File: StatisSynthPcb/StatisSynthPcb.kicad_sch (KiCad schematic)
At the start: 6 parts, among them SW1 SW_Push, SW2 SW_Push

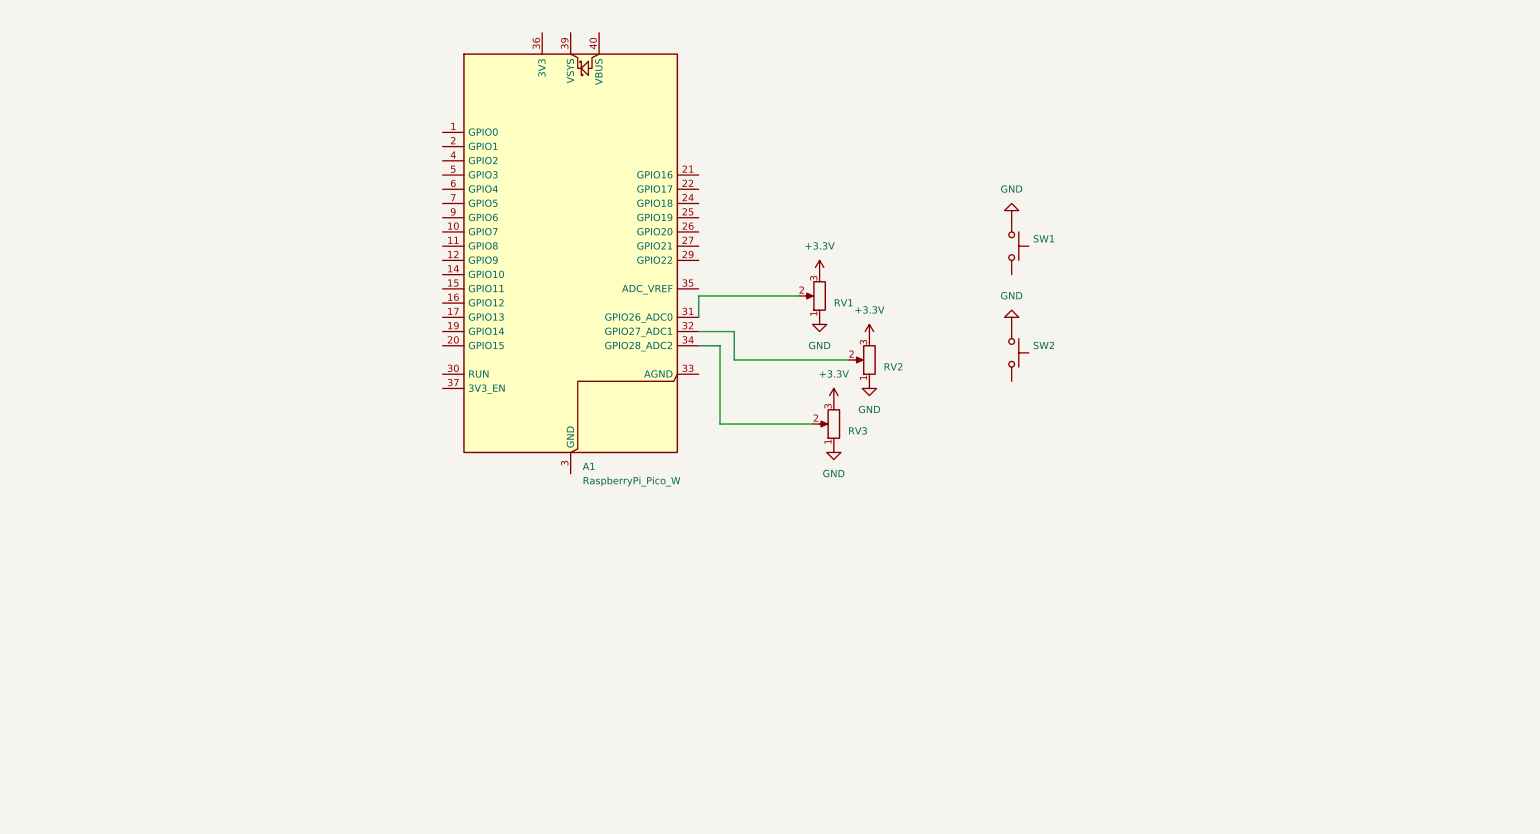
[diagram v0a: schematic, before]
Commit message: made first pcb version
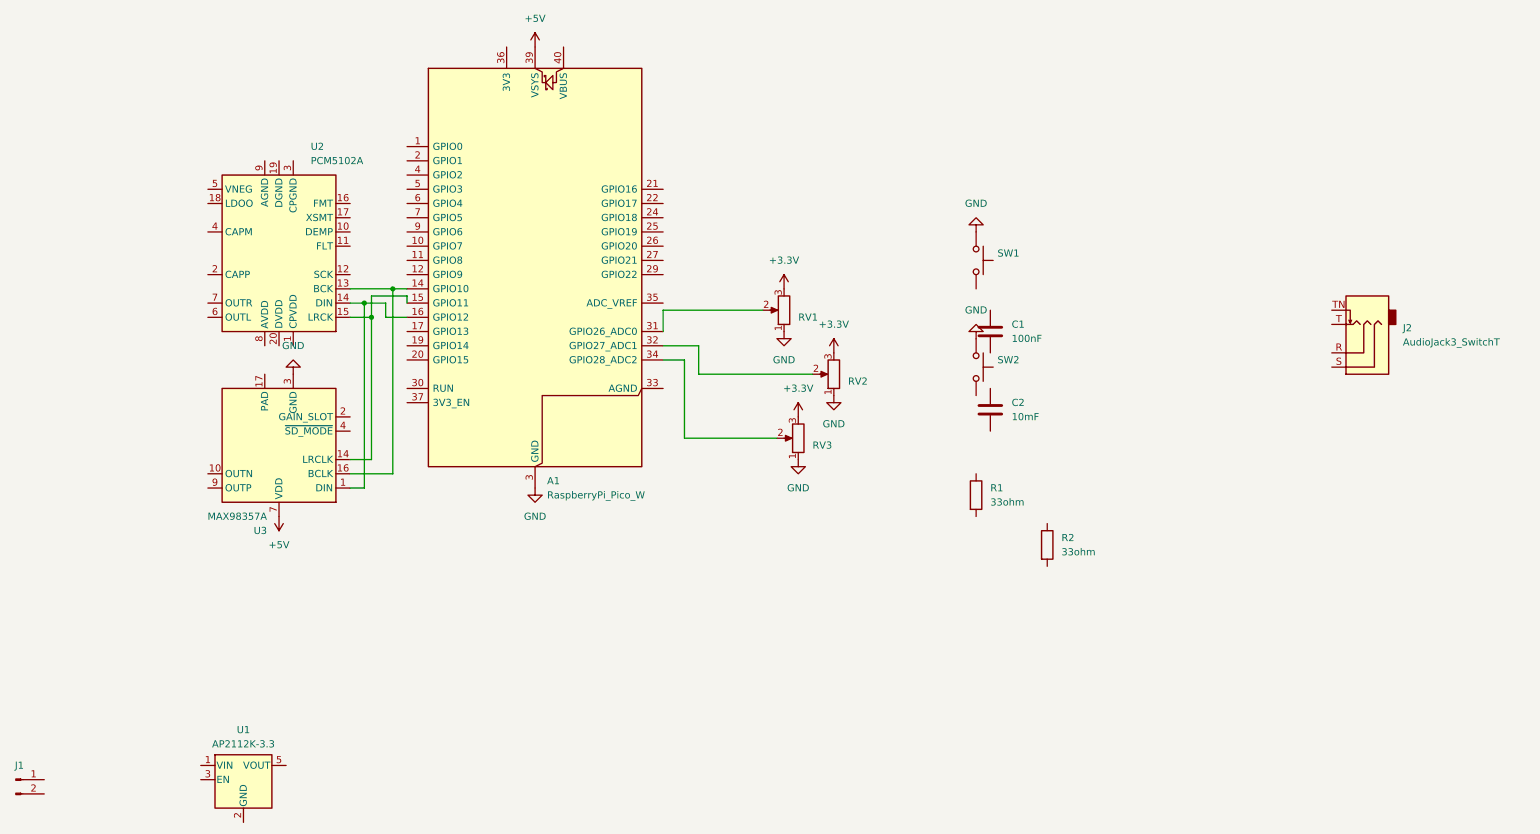
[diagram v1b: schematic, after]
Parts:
- added C1: 100nF, Capacitor_SMD:C_0402_1005Metric_Pad0.74x0.62mm_HandSolder, symbol Device:C
- added C2: 10mF, Capacitor_SMD:C_0805_2012Metric_Pad1.18x1.45mm_HandSolder, symbol Device:C
- added J1: Conn_01x02_Pin, Connector_JST:JST_PH_S2B-PH-K_1x02_P2.00mm_Horizontal, symbol Connector:Conn_01x02_Pin
- added J2: AudioJack3_SwitchT, Connector_Audio:Jack_3.5mm_CUI_SJ-3523-SMT_Horizontal, symbol Connector_Audio:AudioJack3_SwitchT
- added R1, R2: 33ohm, Resistor_SMD:R_0402, symbol Device:R
- added U1: AP2112K-3.3, Package_TO_SOT_SMD:SOT-23-5_HandSoldering, symbol Regulator_Linear:AP2112K-3.3
- added U2: PCM5102A, Package_SO:TSSOP-20_4.4x6.5mm_P0.65mm, symbol Audio:PCM5102A
- added U3: MAX98357A, Package_DFN_QFN:TQFN-16-1EP_3x3mm_P0.5mm_EP1.23x1.23mm, symbol Audio:MAX98357A
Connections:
- net GND: now also A1.13 (GND), A1.18 (GND), A1.23 (GND), A1.28 (GND), A1.3 (GND), A1.38 (GND), A1.8 (GND), U3.11 (GND), U3.15 (GND), U3.3 (GND)
- net at A1.14 (GPIO10): now also U2.13 (BCK), U3.16 (BCLK)
- net at A1.15 (GPIO11): now also U2.15 (LRCK), U3.14 (LRCLK)
- net at A1.16 (GPIO12): now also U2.14 (DIN), U3.1 (DIN)
- net +5V: now reaches A1.39 (VSYS)
- net +5V: now also U3.7 (VDD), U3.8 (VDD)
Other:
- moved on the sheet: A1, RV1, RV2, RV3, SW1, SW2

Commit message: change in schematic
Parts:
- removed C1: 100nF, Capacitor_SMD:C_0402_1005Metric_Pad0.74x0.62mm_HandSolder, symbol Device:C
- removed C2: 10mF, Capacitor_SMD:C_0805_2012Metric_Pad1.18x1.45mm_HandSolder, symbol Device:C
- removed J2: AudioJack3_SwitchT, Connector_Audio:Jack_3.5mm_CUI_SJ-3523-SMT_Horizontal, symbol Connector_Audio:AudioJack3_SwitchT
- removed R2: 33ohm, Resistor_SMD:R_0402, symbol Device:R
- removed U1: AP2112K-3.3, Package_TO_SOT_SMD:SOT-23-5_HandSoldering, symbol Regulator_Linear:AP2112K-3.3
- removed U3: MAX98357A, Package_DFN_QFN:TQFN-16-1EP_3x3mm_P0.5mm_EP1.23x1.23mm, symbol Audio:MAX98357A
- added C3, C5, C6, C7, C8: 100nF, Capacitor_SMD:C_0805_2012Metric_Pad1.18x1.45mm_HandSolder, symbol Device:C
- added C4: 1mikroF, Capacitor_SMD:C_0805_2012Metric_Pad1.18x1.45mm_HandSolder, symbol Device:C
- added D1: D_Schottky, Diode_SMD:D_SOD-123, symbol Device:D_Schottky
- added D2: LED, symbol Device:LED
- added F1: 500ma, Fuse:Fuse_1812_4532Metric_Pad1.30x3.40mm_HandSolder, symbol Device:Polyfuse
- added J2: PCM5102A, symbol Connector:Conn_01x06_Pin
- added J3: Oled, Connector_PinSocket_2.54mm:PinSocket_1x04_P2.54mm_Vertical, symbol Connector:Conn_01x04_Pin
- added J5: InputPAM8403, symbol Connector:Conn_01x05_Pin
- added R3: 100k, Resistor_THT:R_Axial_DIN0207_L6.3mm_D2.5mm_P7.62mm_Horizontal, symbol Device:R
- added R4: 390k, Resistor_THT:R_Axial_DIN0207_L6.3mm_D2.5mm_P7.62mm_Horizontal, symbol Device:R
- added RV4: R_Potentiometer, Potentiometer_THT:Potentiometer_Alps_RK09K_Single_Vertical, symbol Device:R_Potentiometer
- added SW3, SW4: SW_Push, Button_Switch_THT:SW_PUSH_6mm, symbol Switch:SW_Push
- added U3: MCP3208, Package_DIP:DIP-16_W7.62mm_Socket_LongPads, symbol Analog_ADC:MCP3208
- R1: value 33ohm -> Green 220Ω; footprint Resistor_SMD:R_0402 -> (none)
- RV1, RV2, RV3: footprint (none) -> Potentiometer_THT:Potentiometer_Alps_RK09K_Single_Vertical
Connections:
- net +3.3V: now also A1.36 (3V3), U2.17 (XSMT), U2.20 (DVDD), U2.8 (AVDD), C6.2, C8.2, J2.6 (Pin_6), J3.1 (Pin_1), RV4.3, U3.15 (Vref), U3.16 (Vdd)
- net +5V: now also J5.2 (Pin_2); no longer A1.39 (VSYS)
- net GND: now also J1.2 (Pin_2), U2.10 (DEMP), U2.11 (FLT), U2.12 (SCK), U2.16 (FMT), U2.19 (DGND), U2.3 (CPGND), U2.9 (AGND), C3.2, C5.1, C6.1, C7.1, C8.1, D2.1 (K), J2.1 (Pin_1), J2.5 (Pin_5), J3.2 (Pin_2), J5.1 (Pin_1), J5.4 (Pin_4), R4.2, RV4.1, SW3.1, SW4.1, U3.14 (AGND), U3.9 (DGND)
- net BUTTON1: now reaches SW1.2
- net BUTTON1: now also A1.26 (GPIO20)
- net at U2.1 (CPVDD): now also C3.1
- net at A1.14 (GPIO10): no longer U2.13 (BCK)
- net at A1.16 (GPIO12): no longer U2.14 (DIN)
- net at A1.15 (GPIO11): no longer U2.15 (LRCK)
- net at U2.18 (LDOO): now also C7.2
- net at U2.2 (CAPP): now also C4.2
- net at U2.4 (CAPM): now also C4.1
- net at U2.5 (VNEG): now also C5.2
- net at U2.6 (OUTL): now also J5.5 (Pin_5)
- net at U2.7 (OUTR): now also J5.3 (Pin_3)
- net LRCK: now reaches A1.34 (GPIO28_ADC2)
- net LRCK: now also J2.4 (Pin_4); no longer RV3.2
- net DIN1: now reaches A1.31 (GPIO26_ADC0)
- net DIN1: now also U2.14 (DIN), J2.3 (Pin_3); no longer RV1.2
- net BUTTON4: now reaches A1.17 (GPIO13)
- net BUTTON4: now also SW4.2
- net DOUT: now reaches A1.21 (GPIO16)
- net DOUT: now also U3.12 (Dout)
- net CS: now reaches A1.22 (GPIO17)
- net CS: now also U3.10 (~{CS}/SHDN)
- net DIN: now reaches A1.24 (GPIO18)
- net DIN: now also U3.11 (Din)
- net CLK: now reaches A1.25 (GPIO19)
- net CLK: now also U3.13 (CLK)
- net BUTTON2: now reaches A1.27 (GPIO21)
- net BUTTON2: now also SW2.2
- net BUTTON3: now reaches A1.29 (GPIO22)
- net BUTTON3: now also SW3.2
- net BCK: now reaches A1.32 (GPIO27_ADC1)
- net BCK: now also J2.2 (Pin_2); no longer RV2.2
- net at J1.1 (Pin_1): now also F1.1
- net VSYS: now reaches R1.1
- net VSYS: now also A1.39 (VSYS), D1.1 (K), R3.2
- net at R1.2: now also D2.2 (A)
- new net: D1.2 (A), F1.2
- new net ADC_BAT: R3.1, R4.1, U3.8 (CH7)
- new net POT1: RV1.2, U3.1 (CH0)
- new net POT2: RV2.2, U3.2 (CH1)
- new net POT3: RV3.2, U3.3 (CH2)
- new net POT4: RV4.2, U3.4 (CH3)
- new net SCL: J3.4 (Pin_4), U2.15 (LRCK)
- new net SDA: J3.3 (Pin_3), U2.13 (BCK)
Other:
- note added: "ADC channel expansion"
- note added: "Battery Power"
- note added: "Display"
- note added: "GND"
- note added: "If voltage is 4v and resistance 220Ω and the battery voltage is 2.1V, then the output current is roughly 8.6 milliampere"
- note added: "MCU"
- note added: "SCL"
- note added: "SDA"
- note added: "Sound Generation"
- note added: "Switches and potenciometeres"
- note added: "VCC"
- note added: "pins for PCM5102A"
- moved on the sheet: A1, J1, RV1, RV2, RV3, SW1, SW2

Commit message: changed pcb fuse, diode etc
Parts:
- removed C3, C5, C6, C7, C8: 100nF, Capacitor_SMD:C_0805_2012Metric_Pad1.18x1.45mm_HandSolder, symbol Device:C
- removed C4: 1mikroF, Capacitor_SMD:C_0805_2012Metric_Pad1.18x1.45mm_HandSolder, symbol Device:C
- removed F1: 500ma, Fuse:Fuse_1812_4532Metric_Pad1.30x3.40mm_HandSolder, symbol Device:Polyfuse
- removed U2: PCM5102A, Package_SO:TSSOP-20_4.4x6.5mm_P0.65mm, symbol Audio:PCM5102A
- added C1: 100microFarad, Capacitor_THT:CP_Radial_D6.3mm_P2.50mm, symbol Device:C_Polarized
- added F2: Littelfuse 0451002.MRL 2A, symbol Device:Fuse
- added J4: Conn_01x01_Pin, Connector_PinSocket_2.54mm:PinSocket_1x01_P2.54mm_Vertical, symbol Connector:Conn_01x01_Pin
- added RV5: R_Potentiometer, Potentiometer_THT:Potentiometer_Alps_RK09K_Single_Vertical, symbol Device:R_Potentiometer
- added SW5: SW_SPST, Button_Switch_THT:SW_DIP_SPSTx01_Slide_9.78x4.72mm_W7.62mm_P2.54mm, symbol Switch:SW_SPST
- D1: value D_Schottky -> SS34 (SMA)3A; footprint Diode_SMD:D_SOD-123 -> Fuse:Fuseholder_Cylinder-5x20mm_Bulgin_FX0457_Horizontal_Closed
- J2: footprint (none) -> Connector_PinSocket_2.54mm:PinSocket_1x06_P2.54mm_Vertical
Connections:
- net +3.3V: now also RV5.3
- net GND: now also J1.1 (Pin_1), C1.2, RV5.1; no longer J1.2 (Pin_2), J5.1 (Pin_1), J5.4 (Pin_4)
- net SCL: now also A1.7 (GPIO5), J3.3 (Pin_3); no longer J3.4 (Pin_4)
- net SDA: now also A1.6 (GPIO4), J3.4 (Pin_4); no longer J3.3 (Pin_3)
- net VSYS: now also C1.1, J4.1 (Pin_1)
- net at D1.2 (A): now also F2.2
- net POT5: now reaches U3.5 (CH4)
- net POT5: now also RV5.2
- net +5V: no longer names the net of J5.2 (Pin_2)
- new net: J1.2 (Pin_2), SW5.1 (A)
- new net: F2.1, SW5.2 (B)
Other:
- note added: "2040 speaker 4ohm"
- note removed: "Sound Generation"
- moved on the sheet: D2, J1, J5, R1, R3, R4

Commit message: chnages to code and pcb
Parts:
- D1: value SS34 (SMA)3A -> 1N5822; footprint Fuse:Fuseholder_Cylinder-5x20mm_Bulgin_FX0457_Horizontal_Closed -> Diode_THT:D_DO-201AD_P15.24mm_Horizontal
- F2: value Littelfuse 0451002.MRL 2A -> Littelfuse 02301002H; footprint (none) -> Fuse:Fuseholder_Cylinder-5x20mm_Schurter_0031_8201_Horizontal_Open
- J4: value Conn_01x01_Pin -> Conn pin for power amplifier
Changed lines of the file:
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@@
 			)
 		)
-		(property "Value" "Conn_01x01_Pin"
-			(at 77.47 161.036 90)
-			(show_name no)
-			(do_not_autoplace no)
-			(effects
-				(font
-					(size 1.27 1.27)
+		(property "Value" "Conn pin for power amplifier"
+			(at 69.342 161.036 90)
+			(show_name no)
+			(do_not_autoplace no)
+			(effects
+				(font
+					(size 0.762 0.762)
 				)
 				(justify left)
@@
 			)
 		)
-		(property "Value" "SS34 (SMA)3A"
+		(property "Value" "1N5822"
 			(at 60.706 164.338 0)
 			(show_name no)
@@
 			)
 		)
-		(property "Footprint" "Fuse:Fuseholder_Cylinder-5x20mm_Bulgin_FX0457_Horizontal_Closed"
+		(property "Footprint" "Diode_THT:D_DO-201AD_P15.24mm_Horizontal"
 			(at 66.04 168.91 0)
 			(hide yes)
@@
 			)
 		)
-		(property "Value" "Littelfuse 0451002.MRL 2A"
+		(property "Value" "Littelfuse 02301002H"
 			(at 44.196 167.132 90)
 			(show_name no)
@@
 			)
 		)
-		(property "Footprint" ""
+		(property "Footprint" "Fuse:Fuseholder_Cylinder-5x20mm_Schurter_0031_8201_Horizontal_Open"
 			(at 55.88 170.688 90)
 			(hide yes)

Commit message: pcb change
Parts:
- removed D2: LED, symbol Device:LED
- removed J5: InputPAM8403, symbol Connector:Conn_01x05_Pin
- removed R1: Green 220Ω, symbol Device:R
- R4: value 390k -> 330k
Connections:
- no-connect marks 0 -> 16
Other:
- note added: "InputPAM8403"
- note removed: "If voltage is 4v and resistance 220Ω and the battery voltage is 2.1V, then the output current is roughly 8.6 milliampere"

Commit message: added gerbers photos bom
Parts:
- removed SW5: SW_SPST, Button_Switch_THT:SW_DIP_SPSTx01_Slide_9.78x4.72mm_W7.62mm_P2.54mm, symbol Switch:SW_SPST
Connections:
- net at J1.2 (Pin_2): now also F2.1
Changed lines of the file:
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@@
 	(wire
 		(pts
-			(xy 49.53 179.07) (xy 49.53 182.88)
+			(xy 49.53 168.91) (xy 49.53 182.88)
 		)
 		(stroke
@@
 					(unit 1)
 				)
-			)
-		)
-	)
-	(symbol
-		(lib_id "Switch:SW_SPST")
-		(at 49.53 173.99 90)
-		(unit 1)
-		(body_style 1)
-		(exclude_from_sim no)
-		(in_bom yes)
-		(on_board yes)
-		(in_pos_files yes)
-		(dnp no)
-		(property "Reference" "SW5"
-			(at 47.244 174.752 90)
-			(show_name no)
-			(do_not_autoplace no)
-			(effects
-				(font
-					(size 1.27 1.27)
-				)
-				(justify left)
-			)
-		)
-		(property "Value" "SW_SPST"
-			(at 47.244 172.212 90)
-			(show_name no)
-			(do_not_autoplace no)
-			(effects
-				(font
-					(size 1.27 1.27)
-				)
-				(justify left)
-			)
-		)
-		(property "Footprint" "Button_Switch_THT:SW_DIP_SPSTx01_Slide_9.78x4.72mm_W7.62mm_P2.54mm"
-			(at 49.53 173.99 0)
-			(hide yes)
-			(show_name no)
-			(do_not_autoplace no)
-			(effects
-				(font
-					(size 1.27 1.27)
-				)
-			)
-		)
-		(property "Datasheet" ""
-			(at 49.53 173.99 0)
-			(hide yes)
-			(show_name no)
-			(do_not_autoplace no)
-			(effects
-				(font
-					(size 1.27 1.27)
-				)
-			)
-		)
-		(property "Description" "Single Pole Single Throw (SPST) switch"
-			(at 49.53 173.99 0)
-			(hide yes)
-			(show_name no)
-			(do_not_autoplace no)
-			(effects
-				(font
-					(size 1.27 1.27)
-				)
-			)
-		)
-		(pin "1"
-		)
-		(pin "2"
-		)
-		(instances
-			(project "StatisSynthPcb"
-				(path "/b57d530a-5173-4e03-a844-1cb39fed83ec"
-					(reference "SW5")
-					(unit 1)
-				)
